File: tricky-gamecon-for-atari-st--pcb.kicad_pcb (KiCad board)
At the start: 2 copper layers, 109.2 x 45.7 mm, 24 parts, among them J1 Conn_01x09, SW1 GrayHill_series_78_SPDT_DIP_x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, SW2 SW_SPST, SW3 SW_SPST, SW4 SW_SPST, SW5 SW_SPST, SW6 SW_SPST, SW7 SW_SPST, SW8 SW_SPST, SW9 SW_SPST

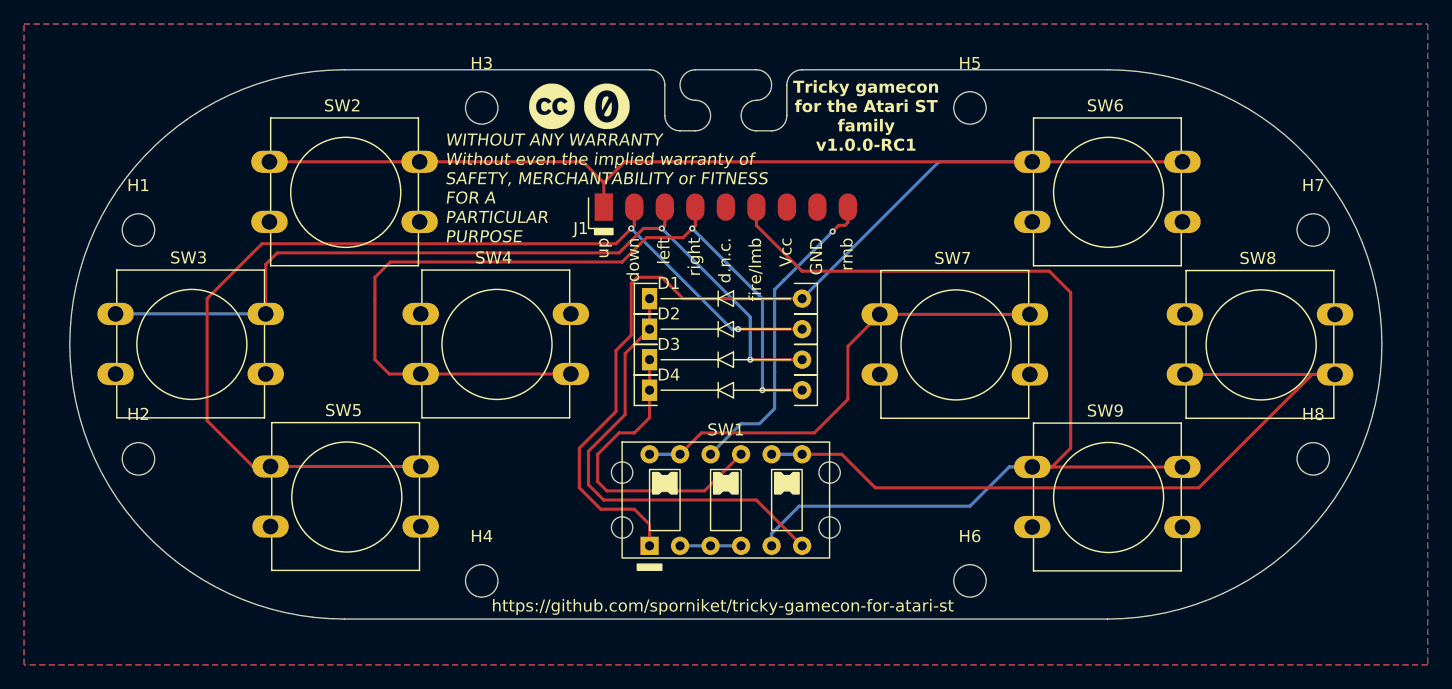
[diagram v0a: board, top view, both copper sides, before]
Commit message: change special2 from left+right to down
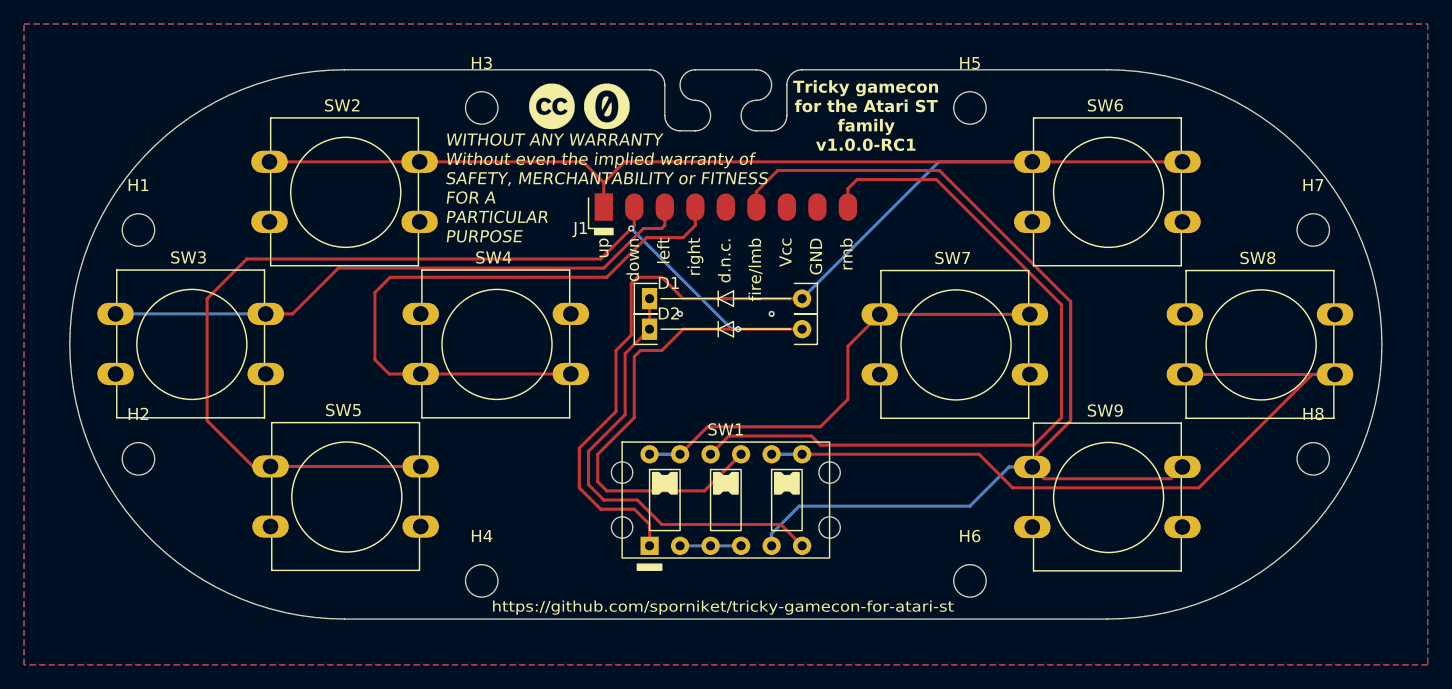
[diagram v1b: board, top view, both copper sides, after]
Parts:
- removed D3, D4: 1N4148, commons-passives_THT:Passive_THT_diode_W2.54mm_L12.70mm
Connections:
- SW1 pad 9: Net-(D3-K) -> /down
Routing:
- net /rmb: track 26.5 -> 64.4 mm, vias 1 -> 0
- net /down: track 86.8 -> 121.6 mm
- net Net-(D3-K): track 26.2 -> 0.00 mm
- net /left: track 71.0 -> 50.3 mm, vias 2 -> 0
- net /right: track 72.8 -> 52.9 mm, vias 2 -> 0
- net /fire/lmb: track 84.3 -> 86.5 mm
- net GND: vias 0 -> 2
